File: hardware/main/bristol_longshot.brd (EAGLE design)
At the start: 12 x 50 mm, 42 parts, among them U1 SAM_D20E, U2 SI4060, U4 ADP1607ACPZN-R7, U5 S25FS-S

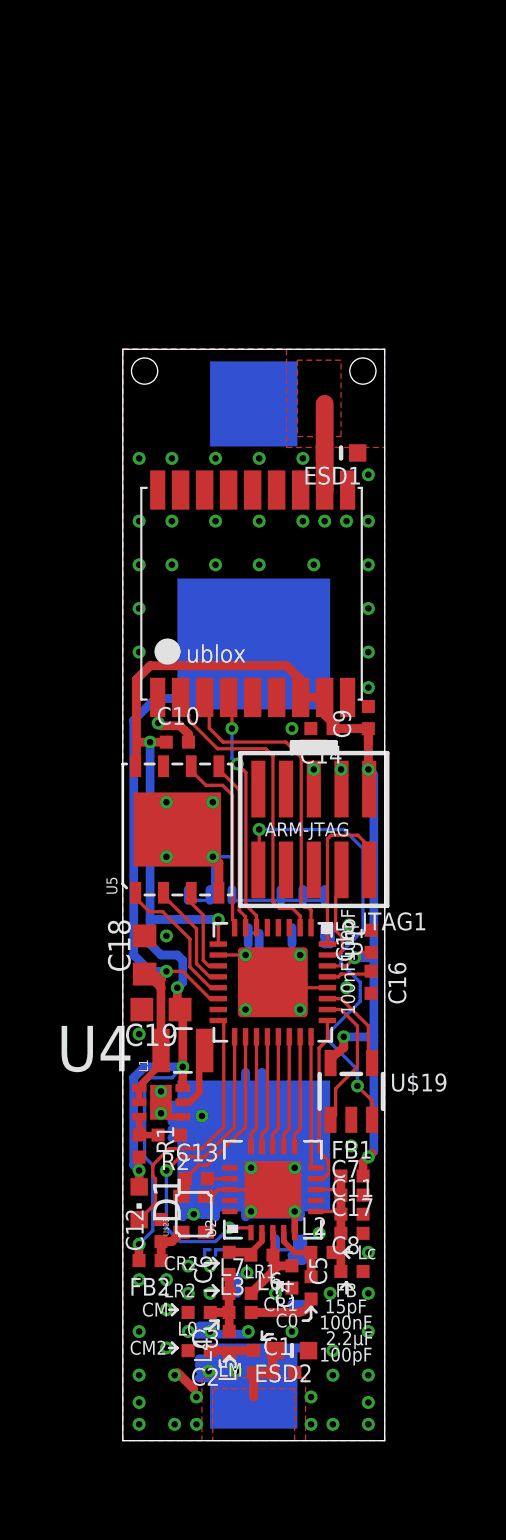
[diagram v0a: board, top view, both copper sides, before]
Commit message: Moved main hardware into subfolder
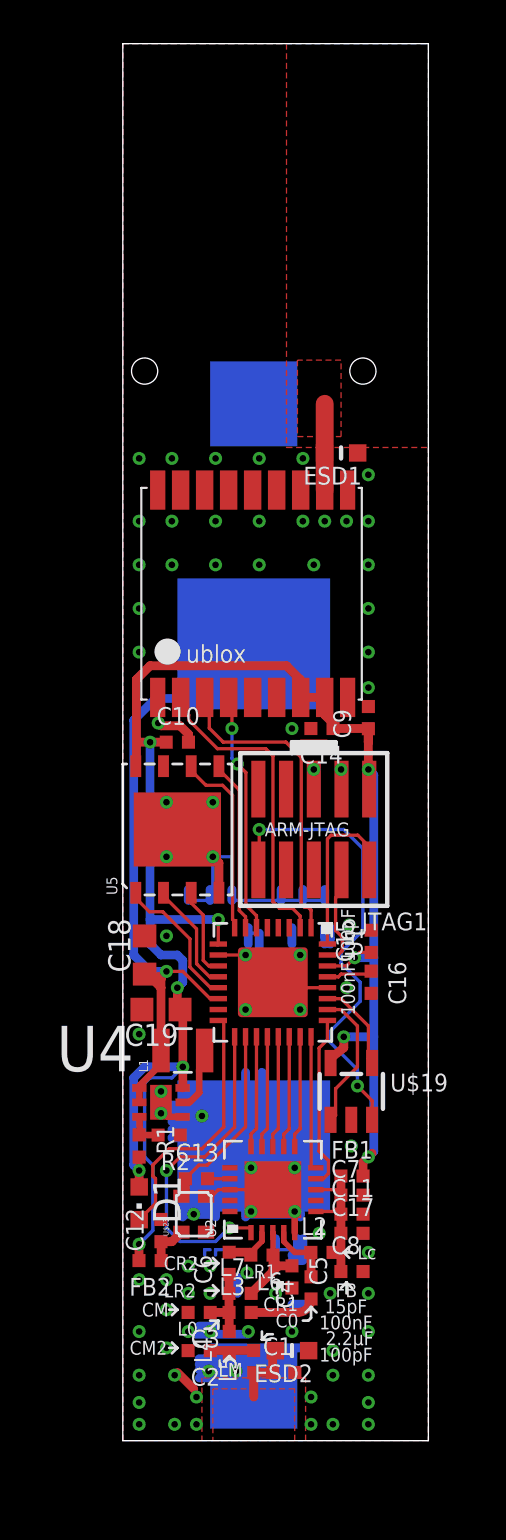
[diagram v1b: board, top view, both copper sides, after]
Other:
- board size 12 x 50 mm -> 14 x 64 mm
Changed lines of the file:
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@@
 <setting verticaltext="up"/>
 </settings>
-<grid distance="0.125" unitdist="mm" unit="mm" style="lines" multiple="1" display="yes" altdistance="0.025" altunitdist="inch" altunit="inch"/>
+<grid distance="1" unitdist="mm" unit="mm" style="lines" multiple="1" display="yes" altdistance="0.025" altunitdist="inch" altunit="inch"/>
 <layers>
 <layer number="1" name="Top" color="4" fill="1" visible="yes" active="yes"/>
@@
 <vertex x="0.5" y="0.5"/>
 </polygon>
-<wire x1="0" y1="0" x2="0" y2="50" width="0" layer="20"/>
-<wire x1="0" y1="50" x2="12" y2="50" width="0" layer="20"/>
-<wire x1="12" y1="50" x2="12" y2="0" width="0" layer="20"/>
-<wire x1="12" y1="0" x2="0" y2="0" width="0" layer="20"/>
+<wire x1="0" y1="0" x2="0" y2="64" width="0" layer="20"/>
+<wire x1="0" y1="64" x2="14" y2="64" width="0" layer="20"/>
+<wire x1="14" y1="64" x2="14" y2="0" width="0" layer="20"/>
+<wire x1="14" y1="0" x2="0" y2="0" width="0" layer="20"/>
 <text x="10.25" y="31.5" size="0.762" layer="113" font="vector" ratio="20" rot="MR90">XxXxXxXxXxXx</text>
 <text x="10" y="24.375" size="0.635" layer="21" font="vector" ratio="16" rot="R270">100nF100pF</text>
@@
 <signal name="GND">
 <polygon width="0.2032" layer="1" isolate="0.2">
-<vertex x="0" y="50"/>
-<vertex x="7.5" y="50"/>
+<vertex x="0" y="64"/>
+<vertex x="7.5" y="64"/>
 <vertex x="7.5" y="45.5"/>
-<vertex x="12" y="45.5"/>
-<vertex x="12" y="0"/>
+<vertex x="14" y="45.5"/>
+<vertex x="14" y="0"/>
 <vertex x="8.375" y="0"/>
 <vertex x="8.375" y="2.875"/>
@@
 </polygon>
 <polygon width="0.2032" layer="16" isolate="0.2">
-<vertex x="0" y="50"/>
-<vertex x="12" y="50"/>
-<vertex x="12" y="0"/>
+<vertex x="0" y="64"/>
+<vertex x="14" y="64"/>
+<vertex x="14" y="0"/>
 <vertex x="0" y="0"/>
 </polygon>

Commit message: Much layout done for new frontpanel
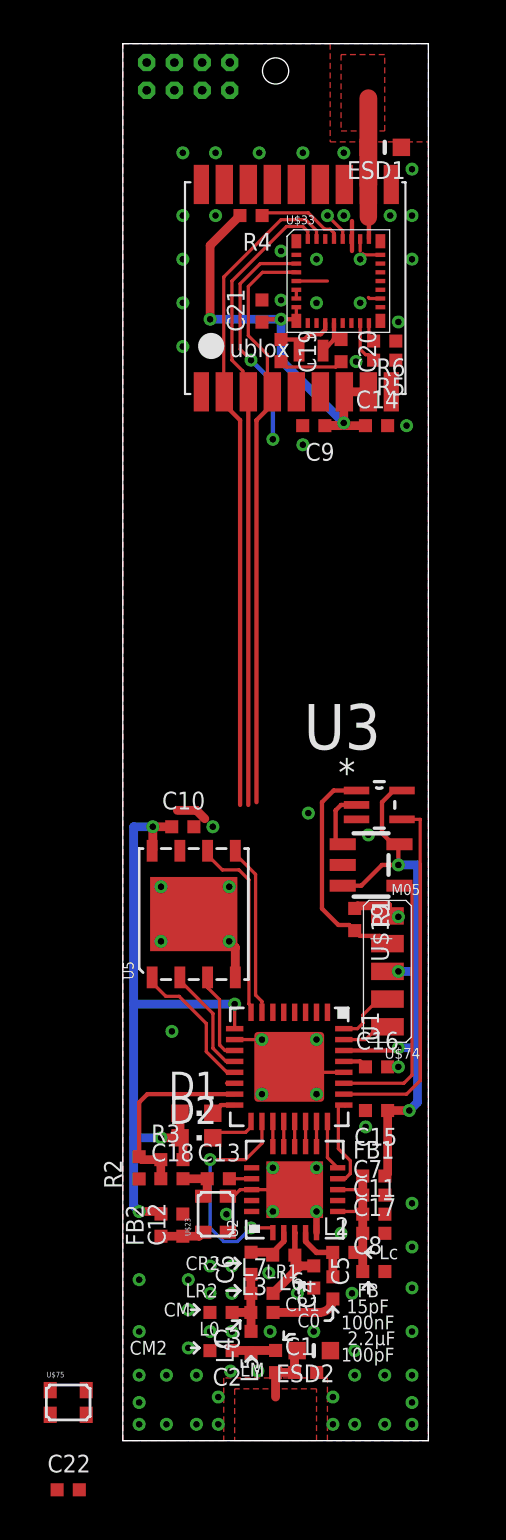
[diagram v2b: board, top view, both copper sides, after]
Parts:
- removed JTAG1: (no value), microbuilder_v3:2X05_1.27MM_SMT
- removed L1: 2.2µH, SparkFun:1007
- removed U$2: AA_HOLDER, fbri:AA
- removed U4: ADP1607ACPZN-R7, ADP1607:DFN200X200X60-7N
- added C20: 18pF, microbuilder_v3:_0402
- added C21, C22: 100nF, microbuilder_v3:_0402
- added D2: GREEN, led:CHIPLED_0603
- added R3: 100kΩ, microbuilder_v3:_0402
- added R4, R5, R6: 10kΩ, microbuilder_v3:_0402
- added U$33: SE880, fbri:SE880
- added U$51: M04X2, fbri:M04X2
- added U$74: M05, fbri:M05_SIDE
- added U$75: TG-5006CJ, fbri:TC-5006CJ
- added U3: SN74LVC1G32DCKR, SN74LVC1G32DCKR:SOT65P210X110-5N
- added Y1: ABS05, fbri:ABS05
- C18: value 10µF -> 100nF; device resistor:C0603K -> microbuilder_v3:_0402
- C19: value 10µF -> 18pF; device resistor:C0603K -> microbuilder_v3:_0402
- R1: value 100kΩ -> 10kΩ
- R2: value 240kΩ -> 100kΩ
- moved C19 30.7 mm to (7.25, 49.9), turned to 270 degrees
- moved R1 14.3 mm to (10.6, 23.9)
- moved ESD1 14.1 mm to (12.0, 59.2)
- moved U$48 14.1 mm to (8.00, 53.0)
- moved C14 14.1 mm to (11.6, 46.5), turned to 0 degrees
- moved C9 13.6 mm to (8.75, 46.5), turned to 180 degrees
- moved U$19 10.4 mm to (11.4, 26.4), turned to 270 degrees
- moved C18 10.3 mm to (2.25, 12.0), turned to 0 degrees
- moved C15 7.75 mm to (11.6, 15.1), turned to 180 degrees
- moved D1 4.89 mm to (3.38, 15.0), turned to 270 degrees
- moved U1 3.95 mm to (7.62, 17.1)
- moved U5 3.95 mm to (3.25, 24.1)
- moved C10 3.88 mm to (2.75, 28.1)
- moved C16 3.88 mm to (11.6, 17.1), turned to 0 degrees
- moved R2 2.03 mm to (0.75, 12.5), turned to 90 degrees
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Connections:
- net LED renamed LED1
- removed net !MR: JTAG1.10, U$19.3
- removed net +2: U$2.+1
- removed net 9_V_RESET: U$48.9_V_RESET
- removed net FB: R1.1, R2.2, U4.3
- removed net SW: L1.2, U4.5
- new net EXT!RESET: R1.2, U$74.$2, U3.1
- new net LED2: D2.C, U1.17
- new net N$2: U$33.$6, U$33.$7
- new net N$3: R6.2, U$33.$17
- new net N$4: R4.1, U$33.$31
- new net N$5: R5.2, U$33.$16
- new net RTC_XI: C19.1, U$33.$12, Y1.1
- new net RTC_XO: C20.1, U$33.$13, Y1.2
- new net SAM_XOSC: C18.1, R2.2, R3.1, U1.15
- new net SE_ON_OFF: U$33.$3, U1.5
- new net VCC: U$75.4
- new net WDI!RESET: U$19.1, U3.2
- net !RESET: now also U$33.$30, U$48.9_V_RESET, U3.4; no longer U$19.1
- net 1.2V: now also U$51.P$5; no longer C18.1, L1.1, U$2.+2, U4.1, U4.2
- net 1.8V: now also C21.1, D2.A, R3.2, R4.2, U$19.3, U$33.$8, U$33.$9, U$51.P$3, U$74.$3, U3.5; no longer C19.1, JTAG1.1, R1.2, U4.6
- net GIMO: now also U$33.$34
- net GND: now also C20.2, C21.2, R1.1, R5.1, R6.1, U$33.$1, U$33.$18, U$33.$20, U$33.$23, U$33.$24, U$33.$25, U$33.$26, U$33.$28, U$33.$29, U$33.$5, U$51.P$1, U$51.P$2, U$74.$1, U$75.2, U3.3; no longer C18.2, JTAG1.3, JTAG1.5, U$2.-1, U$2.-2, U4.4, U4.7
- net GOMI: now also U$33.$33
- net GPS_ANT: now also U$33.$27
- net SI_SDN: now also U1.18; no longer U1.17
- net SWDCLK: now also U$74.$5; no longer JTAG1.4
- net SWDIO: now also U$74.$4; no longer JTAG1.2
- net TCXO_OUT: now also C18.2; no longer U1.18
- net TIMEPULSE: now also U$33.$4
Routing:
- net GND: track 74.6 -> 30.5 mm
- net 1.2V: track 30.5 -> 0.38 mm, vias 1 -> 0
- net !MR: track 21.5 -> 0.00 mm, vias 2 -> 0
- net TIMEPULSE: track 11.0 -> 27.3 mm, vias 2 -> 0
- net GOMI: track 14.5 -> 30.4 mm
- net GIMO: track 14.3 -> 29.3 mm
- net !RESET: track 6.51 -> 17.9 mm, vias 0 -> 1
- net SE_ON_OFF: track 0.00 -> 10.7 mm, vias 0 -> 2
- net LED1: track 12.0 -> 1.41 mm
- net EXT!RESET: track 0.00 -> 10.3 mm
- net SAM_XOSC: track 0.00 -> 8.97 mm
- net WDI: track 4.15 -> 12.5 mm
- net TCXO_OUT: track 8.74 -> 1.98 mm
- net SWDIO: track 8.10 -> 2.78 mm
- net SI_SDN: track 15.5 -> 10.6 mm
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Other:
- board text added: "(C) Richard Meadows 2015"
- board text added: "ARM-SWD"
- board text removed: "(C) Richard Meadows 2014"
- board text removed: "100nF100pF"
- board text removed: "ARM-JTAG"
- board text removed: "XxXxXxXxXxXx"
- board text removed: "ublox"

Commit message: Routing on the bottom half of the main board almost done
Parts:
- added C23: 100nF, microbuilder_v3:_0402
- added R10: 22kΩ, microbuilder_v3:_0402
- added R7, R8, R9: 10kΩ, microbuilder_v3:_0402
- moved C22 55.6 mm to (12.8, 51.2)
- moved U$75 53.3 mm to (12.7, 52.9), turned to 90 degrees
- moved C19 0.50 mm to (6.75, 49.9)
- moved C20 0.50 mm to (9.50, 49.9)
- moved C21 0.50 mm to (5.88, 51.8)
- moved R4 0.50 mm to (5.38, 56.1)
- moved R5 0.50 mm to (11.5, 49.5)
- moved R6 0.50 mm to (11.5, 50.4)
- moved U$33 0.50 mm to (9.38, 53.1)
- moved Y1 0.50 mm to (8.12, 49.9)
- moved C14 0.25 mm to (11.4, 46.5)
- moved C9 0.25 mm to (8.50, 46.5)
- moved ESD1 0.25 mm to (11.8, 59.2)
- moved U$48 0.25 mm to (7.75, 53.0)
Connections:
- removed net VCC: U$75.4
- new net I2C_CLK: R8.1, U$51.P$8, U1.6
- new net I2C_DATA: R7.1, U$51.P$7, U1.5
- new net SE_TCXO_CLK: U$33.$21, U$75.3
- new net SE_VCO_TCXO: C22.1, U$33.$19, U$75.4
- new net VBATT_SENSE: R10.1, R9.2, U1.14
- new net VSOLAR: U$51.P$6, U1.4
- net 1.2V: now also R10.2; no longer U1.14
- net 1.8V: now also C23.1, R7.2, R8.2
- net GND: now also C22.2, C23.2, R9.1
- net SE_ON_OFF: no longer U1.5
- net TIMEPULSE: now also U1.3; no longer U1.6
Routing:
- net I2C_CLK: track 0.00 -> 49.0 mm, vias 0 -> 2
- net VSOLAR: track 0.00 -> 48.0 mm
- net 1.2V: track 0.38 -> 47.9 mm, vias 0 -> 1
- net I2C_DATA: track 0.00 -> 46.9 mm
- net 1.8V: track 83.0 -> 127.4 mm
- net !RESET: track 17.9 -> 35.2 mm
- net TIMEPULSE: track 27.3 -> 41.1 mm
- net GOMI: track 30.4 -> 42.6 mm
- net GIMO: track 29.3 -> 39.5 mm
- net SE_ON_OFF: track 10.7 -> 6.42 mm
- net VBATT_SENSE: track 0.00 -> 2.79 mm
- net SE_VCO_TCXO: track 0.00 -> 1.71 mm
- net SE_TCXO_CLK: track 0.00 -> 1.59 mm
- net GND: track 30.5 -> 30.3 mm, vias 87 -> 89

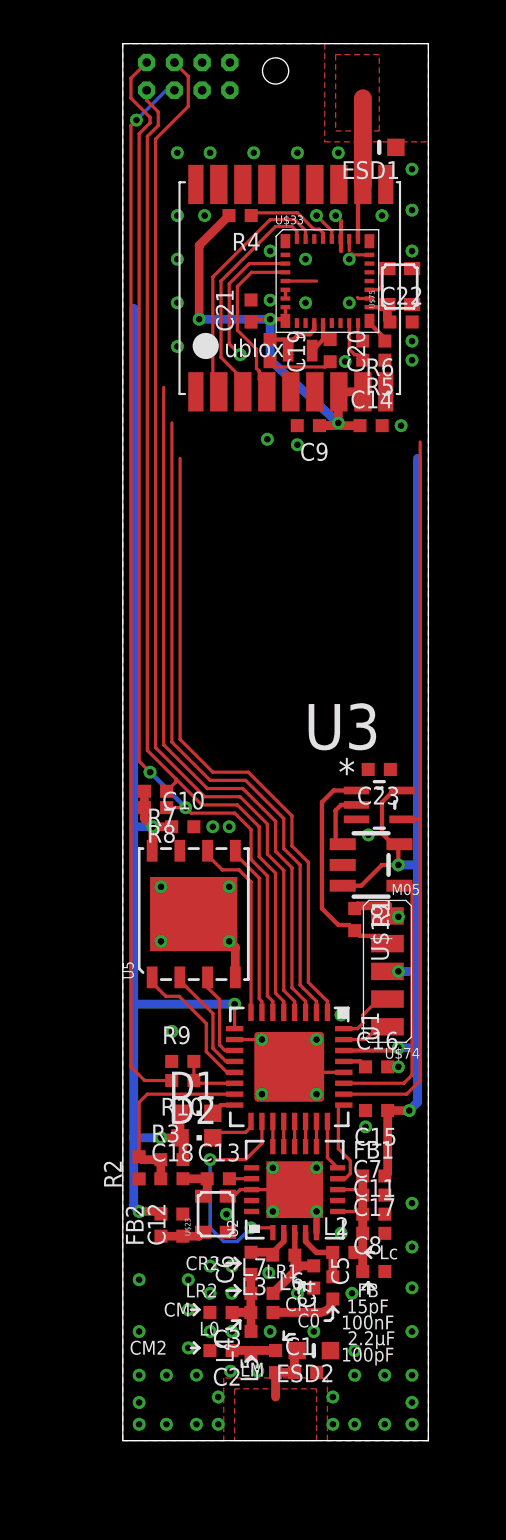
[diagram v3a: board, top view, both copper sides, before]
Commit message: Updated main board to v0.98.0
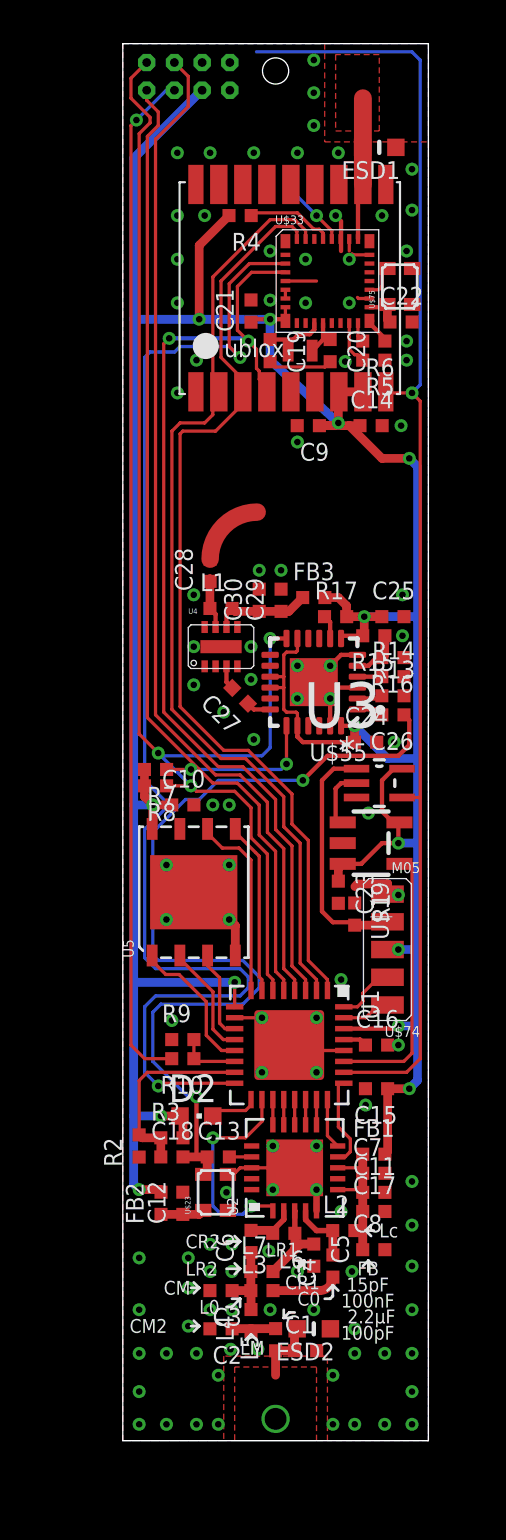
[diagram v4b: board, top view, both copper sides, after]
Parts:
- removed D1: GREEN, led:CHIPLED_0603
- added C24, C25, C26, C27, C28, C29: 100nF, microbuilder_v3:_0402
- added C30: 100pF, microbuilder_v3:_0402
- added FB3: (no value), microbuilder_v3:_0402
- added L1: 100nH, microbuilder_v3:_0402
- added R13, R14: 0Ω, microbuilder_v3:_0402
- added R15, R17: 10kΩ, microbuilder_v3:_0402
- added R16: 15kΩ, microbuilder_v3:_0402
- added U$55: SI5356, si5356:QFN24_4MM
- added U4: AD8354, fbri:LFCSP_VD_8
- moved C23 5.93 mm to (9.88, 25.1), turned to 270 degrees
- moved C1 1.00 mm to (8.38, 4.12)
- moved C10 1.00 mm to (2.75, 29.1)
- moved C11 1.00 mm to (11.5, 11.4)
- moved C12 1.00 mm to (2.75, 10.9)
- moved C13 1.00 mm to (4.38, 13.0)
- moved C15 1.00 mm to (11.6, 16.1)
- moved C16 1.00 mm to (11.6, 18.1)
- moved C17 1.00 mm to (11.5, 10.5)
- moved C18 1.00 mm to (2.25, 13.0)
- moved C2 1.00 mm to (4.50, 5.12)
- moved C3 1.00 mm to (4.50, 6.88)
- moved C4 1.00 mm to (9.62, 8.00)
- moved C5 1.00 mm to (8.75, 8.50)
- moved C6 1.00 mm to (5.88, 9.12)
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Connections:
- removed net I2C_CLK: R8.1, U$51.P$8, U1.6
- removed net I2C_DATA: R7.1, U$51.P$7, U1.5
- removed net LED1: D1.C, U1.16
- new net AMPL_OUT: C28.1, L1.1, U4.7
- new net AMPL_VPOS: C29.1, C30.1, FB3.1, L1.2, U4.6
- new net CLKIN: R14.1, U$55.4
- new net HF: C28.2
- new net HF_CLK: C27.1, U$55.18
- new net INPT: C27.2, U4.3
- new net INTR: R17.1, U$55.8
- new net N$7: U$55.9
- new net SCL: R8.1, U$51.P$8, U$55.12, U1.6
- new net SDA: R7.1, U$51.P$7, U$55.19, U1.5
- new net SSC_DIS: R15.1, R16.2, U$55.5
- new net XA: C26.2, U$55.1
- new net XB: R13.1, U$55.2
- net !RESET: now also U$51.P$4
- net 1.8V: now also C24.1, C25.1, FB3.2, R15.2, R17.2, U$55.11, U$55.15, U$55.16, U$55.20, U$55.24, U$55.7; no longer D1.A
- net GND: now also C24.2, C25.2, C29.2, C30.2, R13.2, R14.2, R16.1, U$55.23, U$55.3, U$55.6, U$55.PAD, U4.1, U4.4, U4.5, U4.8, U4.EPAD
- net SE_ON_OFF: now also U1.16
- net TCXO_OUT: now also C26.1
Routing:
- net SCL: track 0.00 -> 59.1 mm, vias 0 -> 3
- net SDA: track 0.00 -> 52.6 mm, vias 0 -> 2
- net SE_ON_OFF: track 6.42 -> 57.8 mm
- net I2C_CLK: track 49.0 -> 0.00 mm, vias 2 -> 0
- net I2C_DATA: track 46.9 -> 0.00 mm
- net TCXO_OUT: track 1.98 -> 41.8 mm, vias 0 -> 2
- net 1.8V: track 127.4 -> 165.7 mm, vias 11 -> 14
- net !RESET: track 35.2 -> 62.7 mm, vias 1 -> 2
- net GND: track 30.3 -> 36.5 mm, vias 89 -> 109
- net TIMEPULSE: track 41.1 -> 45.8 mm, vias 0 -> 2
- net AMPL_VPOS: track 0.00 -> 4.51 mm
- net GIMO: track 39.5 -> 43.4 mm
- net HF: track 0.00 -> 3.05 mm
- net AMPL_OUT: track 0.00 -> 2.43 mm
- net SSC_DIS: track 0.00 -> 2.33 mm
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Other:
- board text added: "ARM - SWD"
- board text removed: "ARM-SWD"
